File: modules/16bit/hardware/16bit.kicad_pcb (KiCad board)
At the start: 4 copper layers, 29 x 110 mm, 99 parts, among them J1 PJ301M-12, J2 PJ301M-12, J3 PJ301M-12, J4 PJ301M-12, J5 PJ301M-12, J6 Eurorack_2x5, J7 USB-C, Q1 MMBT3904, SW1 MODE, SW2 BOOT, SW3 RUN, U1 RP2350A, U2 W25Q128JVS, U3 APS6404L-3SQR-SN, U4 PT8211, U5 TL074, U6 MCP6002, U7 TL072, U8 AMS1117-5.0, U9 AMS1117-3.3, Y1 12MHz

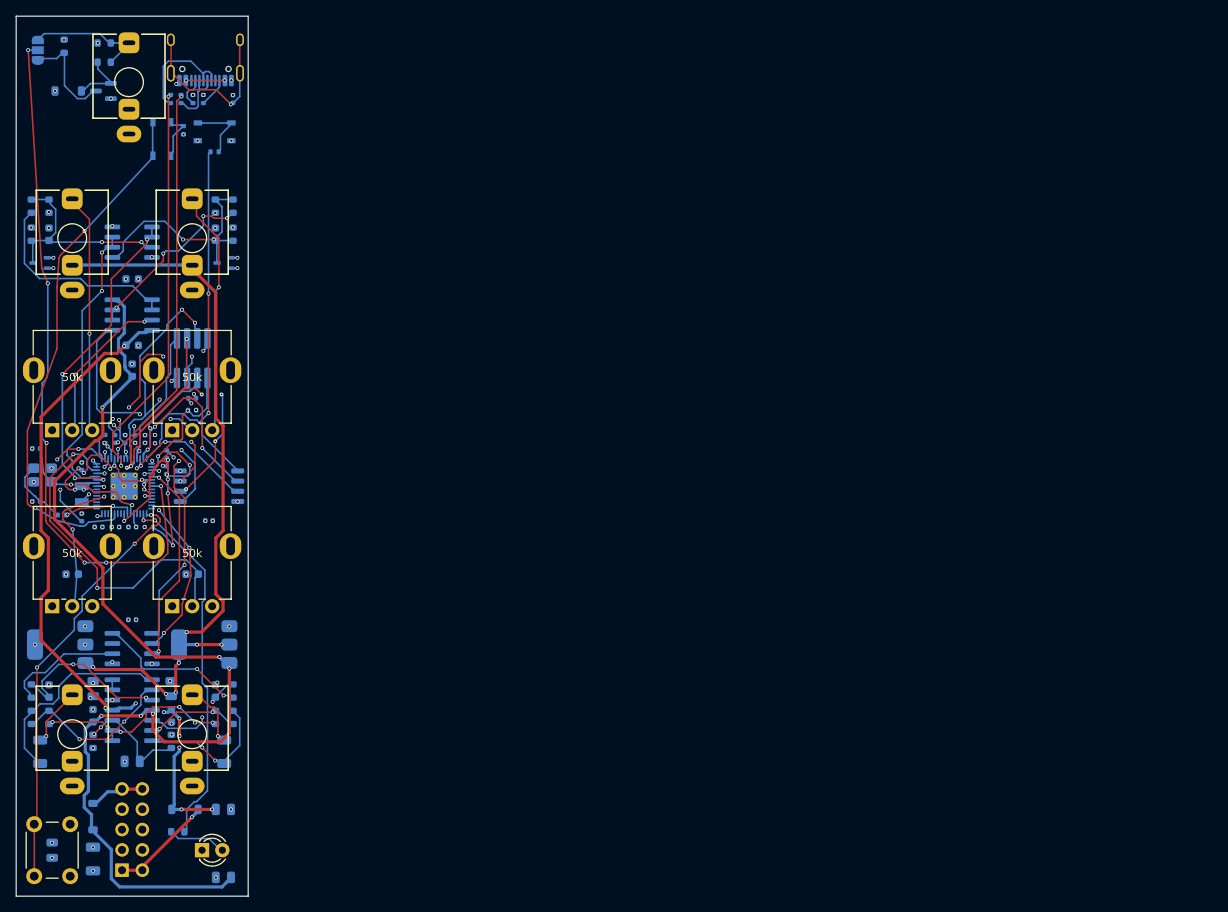
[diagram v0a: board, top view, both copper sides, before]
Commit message: 16bit: start manual re-route; place and route bottom power/output stage
- Strip R1 router copper; move SMD parts off-board for hand placement
- 4-layer stackup (F sig / In1 GND / In2 +3V3 / B sig), Power net class
- Move CV jacks/pots up and to the edge, bottom pots RV3/RV4 to Y128
  (board, panel, geometry.json) to free the middle for the RP2350
- Place and route J6 entry, D2/D3, U8/U9 regulators, U5 output amps,
  VREF divider and outputs to J4/J5 (B.Cu + F.Cu only, no vias in pads)
- Document the no-vias-in-SMD-pads rule for the manual route

Native DRC + schematic parity: 0 violations, 0 parity issues.

Co-Authored-By: Claude Opus 5.5 <noreply@anthropic.com>
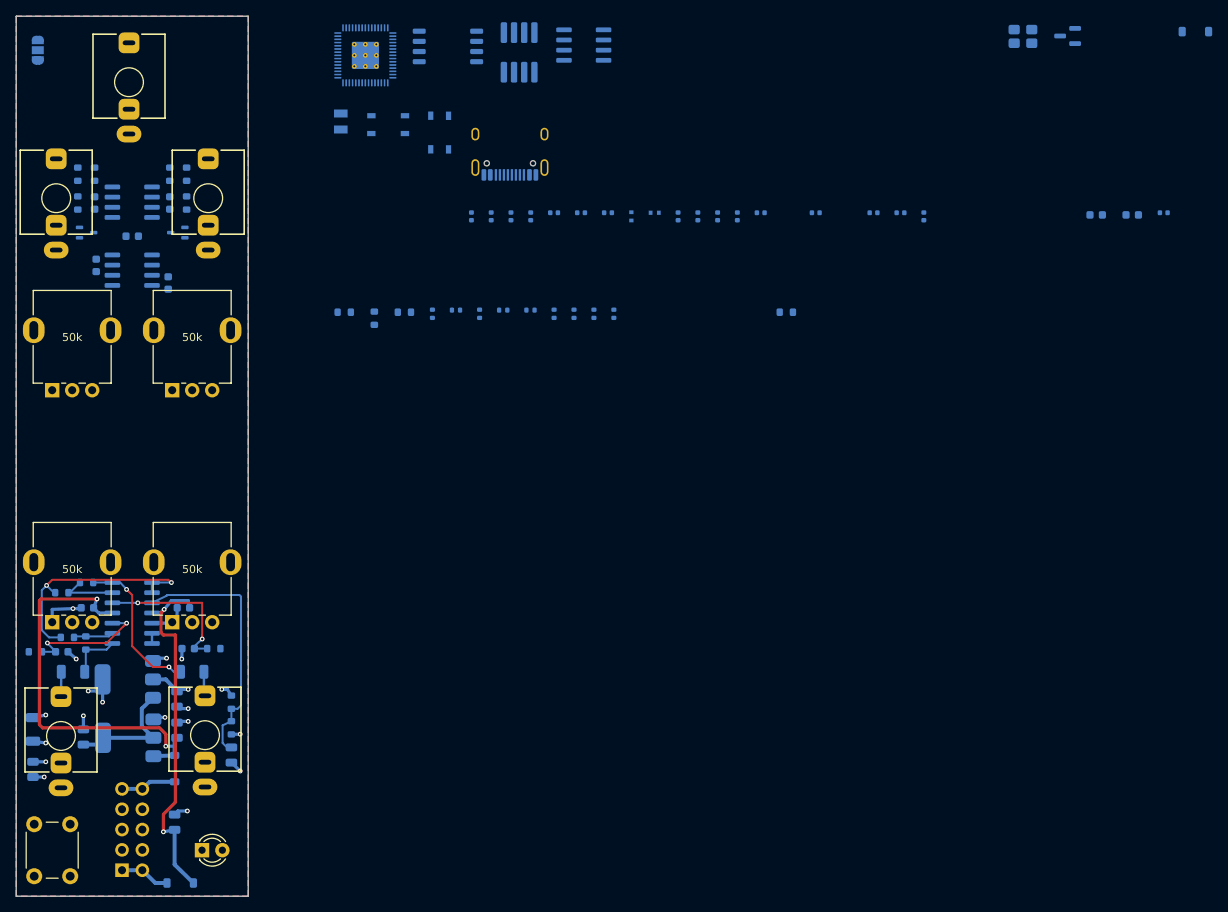
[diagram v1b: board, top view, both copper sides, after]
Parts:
- moved D4 141.1 mm to (247.9, 61.2)
- moved C33 138.6 mm to (243.9, 83.8)
- moved C30 135.6 mm to (235.5, 84.1)
- moved Y1 134.2 mm to (226.3, 61.8)
- moved C31 125.8 mm to (240.0, 84.1)
- moved Q1 120.7 mm to (231.9, 61.7)
- moved C20 103.9 mm to (200.4, 83.8)
- moved R20 100.0 mm to (196.8, 96.2)
- moved C18 95.2 mm to (193.6, 83.8)
- moved U4 94.2 mm to (171.4, 62.9)
- moved C22 91.5 mm to (207.7, 83.8)
- moved C23 91.5 mm to (211.0, 83.8)
- moved C17 90.2 mm to (190.6, 84.3)
- moved C24 87.6 mm to (214.0, 84.3)
- moved C16 85.4 mm to (188.2, 84.3)
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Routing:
- net /MIDI_RX: track 88.3 -> 0.00 mm, vias 6 -> 0
- net +12V_F: track 132.8 -> 50.5 mm, vias 6 -> 2
- net +5V: track 93.4 -> 14.9 mm, vias 7 -> 0
- net +1V1: track 68.7 -> 0.00 mm, vias 16 -> 0
- net /RUN: track 65.4 -> 0.00 mm, vias 2 -> 0
- net /QSPI_SCLK: track 54.2 -> 0.00 mm, vias 7 -> 0
- net /QSPI_SS: track 53.5 -> 0.00 mm, vias 2 -> 0
- net /BUTTON: track 53.4 -> 0.00 mm, vias 3 -> 0
- net /USB_DP: track 50.7 -> 0.00 mm, vias 2 -> 0
- net /USB_DM: track 48.6 -> 0.00 mm, vias 2 -> 0
- net /LED: track 45.5 -> 0.00 mm, vias 2 -> 0
- net /POT4: track 43.8 -> 0.00 mm, vias 2 -> 0
- net /QSPI_SD3: track 42.6 -> 0.00 mm, vias 5 -> 0
- net /QSPI_SD2: track 42.1 -> 0.00 mm, vias 6 -> 0
- net /CV1_ADC: track 41.3 -> 0.00 mm, vias 4 -> 0
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- added copper zone on B.Cu, net GND
- added copper zone on F.Cu, net GND

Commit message: 16bit: add U8 +5V thermal copper (F/B patches, 8 vias)
Co-Authored-By: Claude Opus 5.5 <noreply@anthropic.com>
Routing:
- net +5V: vias 0 -> 8
- added copper zone on B.Cu, net +5V
- added copper zone on F.Cu, net +5V
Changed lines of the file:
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@@
+		)
+	)
+	(via
+		(at 113.5 149.7)
+		(size 0.6)
+		(drill 0.3)
+		(layers "F.Cu" "B.Cu")
+		(net "+5V")
+	)
+	(via
+		(at 115.0 149.7)
+		(size 0.6)
+		(drill 0.3)
+		(layers "F.Cu" "B.Cu")
+		(net "+5V")
+	)
+	(via
+		(at 113.5 151.2)
+		(size 0.6)
+		(drill 0.3)
+		(layers "F.Cu" "B.Cu")
+		(net "+5V")
+	)
+	(via
+		(at 115.0 151.2)
+		(size 0.6)
+		(drill 0.3)
+		(layers "F.Cu" "B.Cu")
+		(net "+5V")
+	)
+	(via
+		(at 113.5 152.7)
+		(size 0.6)
+		(drill 0.3)
+		(layers "F.Cu" "B.Cu")
+		(net "+5V")
+	)
+	(via
+		(at 115.0 152.7)
+		(size 0.6)
+		(drill 0.3)
+		(layers "F.Cu" "B.Cu")
+		(net "+5V")
+	)
+	(via
+		(at 110.5 152.9)
+		(size 0.6)
+		(drill 0.3)
+		(layers "F.Cu" "B.Cu")
+		(net "+5V")
+	)
+	(via
+		(at 112.0 152.9)
+		(size 0.6)
+		(drill 0.3)
+		(layers "F.Cu" "B.Cu")
+		(net "+5V")
+	)
+	(zone
+		(net "+5V")
+		(layer "B.Cu")
+		(name "U8 heat +5V B")
+		(hatch edge 0.5)
+		(priority 1)
+		(connect_pads yes
+			(clearance 0.25)
+		)
+		(min_thickness 0.2)
+		(fill yes
+			(thermal_gap 0.5)
+			(thermal_bridge_width 0.5)
+			(island_removal_mode 0)
+		)
+		(polygon
+			(pts
+				(xy 109.9 145.7) (xy 116.3 145.7) (xy 116.3 154.3) (xy 109.9 154.3)
+			)
+		)
+	)
+	(zone
+		(net "+5V")
+		(layer "F.Cu")
+		(name "U8 heat +5V F")
+		(hatch edge 0.5)
+		(priority 1)
+		(connect_pads yes
+			(clearance 0.25)
+		)
+		(min_thickness 0.2)
+		(fill yes
+			(thermal_gap 0.5)
+			(thermal_bridge_width 0.5)
+			(island_removal_mode 0)
+		)
+		(polygon
+			(pts
+				(xy 108.0 148.75) (xy 118.0 148.75) (xy 118.0 154.3) (xy 108.0 154.3)
+			)
 		)
 	)

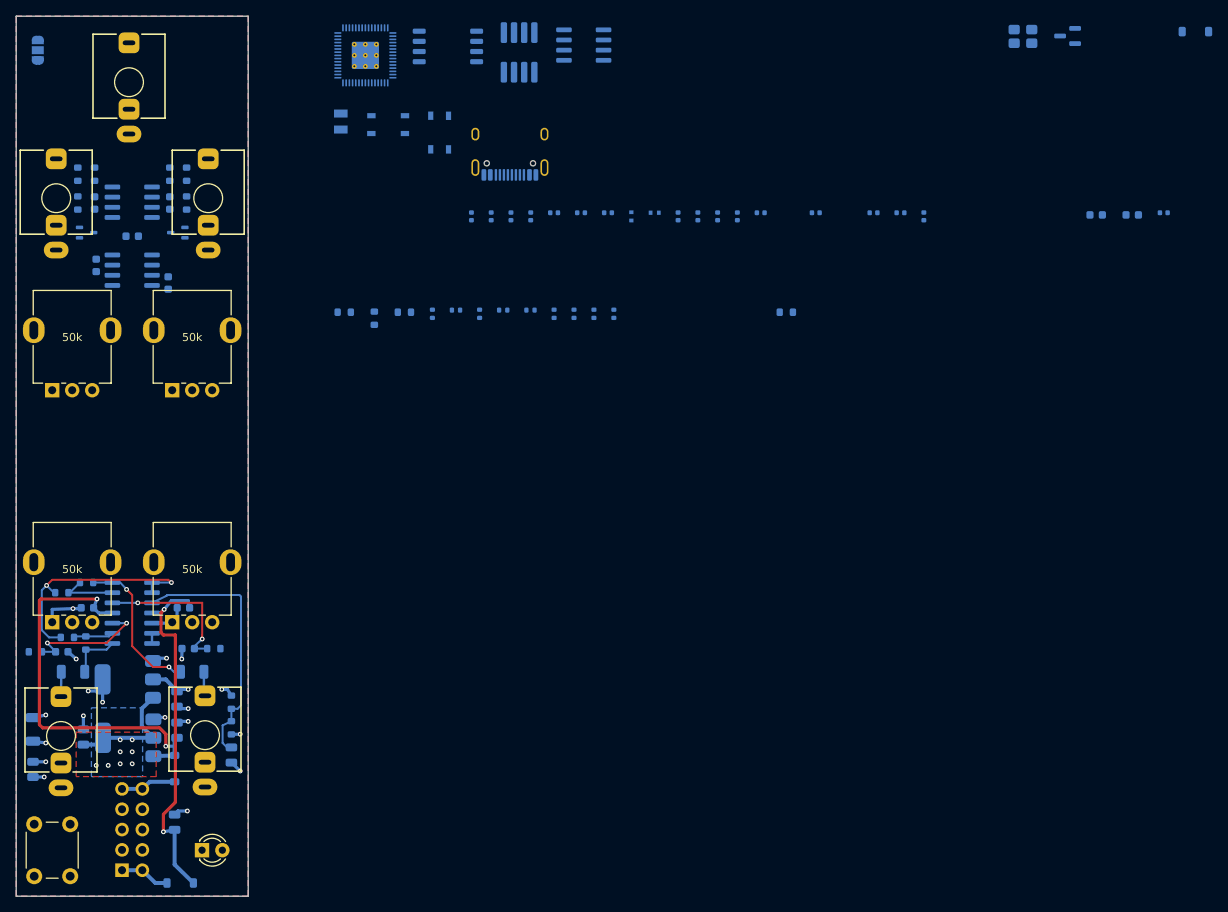
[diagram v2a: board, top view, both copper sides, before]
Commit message: 16bit: place USB-C, MIDI input and CV buffer groups; route their local links
Co-Authored-By: Claude Opus 5.5 <noreply@anthropic.com>
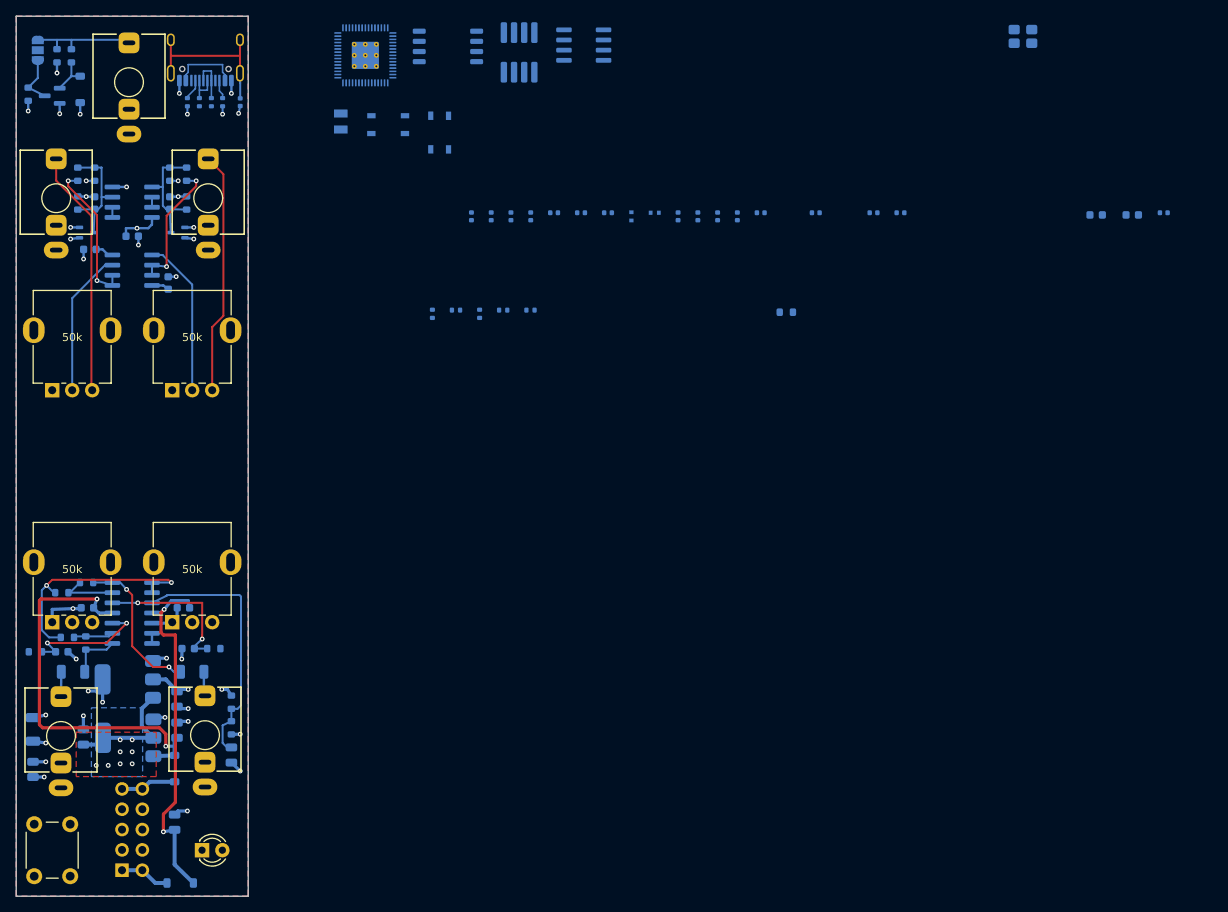
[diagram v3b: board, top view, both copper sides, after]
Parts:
- moved D4 139.6 mm to (108.5, 68.4), turned to -90 degrees
- moved Q1 127.1 mm to (105.0, 69.2)
- moved C24 86.6 mm to (128.5, 70.0), turned to -90 degrees
- moved R11 57.3 mm to (121.9, 70.0), turned to -90 degrees
- moved R12 55.6 mm to (126.3, 70.0), turned to -90 degrees
- moved R3 54.0 mm to (105.6, 64.2), turned to -90 degrees
- moved R10 53.8 mm to (123.4, 70.0), turned to -90 degrees
- moved R2 51.5 mm to (102.0, 69.0), turned to -90 degrees
- moved R9 50.3 mm to (124.9, 70.0), turned to -90 degrees
- moved R1 46.8 mm to (107.4, 64.2), turned to -90 degrees
- moved J7 39.8 mm to (124.2, 63.2)
- moved C29 2.15 mm to (109.7, 88.4), turned to 0 degrees
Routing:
- net /CV1_IN: track 0.00 -> 30.7 mm
- net /CV2_IN: track 0.00 -> 30.3 mm
- net GND: track 26.5 -> 46.9 mm, vias 13 -> 28
- net Net-(J7-SHIELD): track 0.00 -> 20.1 mm
- net Net-(U7B-+): track 0.00 -> 19.8 mm
- net /CV1_AMP: track 0.00 -> 18.4 mm, vias 0 -> 2
- net Net-(U7A-+): track 0.00 -> 18.2 mm
- net /CV2_AMP: track 0.00 -> 16.6 mm, vias 0 -> 2
- net /CV2_BUF: track 0.00 -> 15.2 mm
- net /CV1_BUF: track 0.00 -> 15.2 mm
- net /MIDI_IN: track 0.00 -> 13.9 mm
- net +3V3: track 12.3 -> 24.6 mm, vias 6 -> 13
- net /VBUS: track 0.00 -> 8.54 mm
- net /RX_Q: track 0.00 -> 6.18 mm
- net Net-(J7-D+-PadA6): track 0.00 -> 5.59 mm
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
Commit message: 16bit: place memories, DAC, MCU support, BOOT/RESET; route QSPI, I2S, USB pair, BOOT
- U2 flash / U3 PSRAM beside RP2350, QSPI + PSRAM_CS + I2S on B.Cu with 0 vias
- SW2 BOOT / SW3 RESET at top-left on B.Cu; JP1 MIDI cluster moved 2.6 mm down
- USB D+/D- coupled on F.Cu, 4 vias (2 at port, 2 at MCU)
- U1 regulator corner (L1, C12, C13, C17, R4) and inner power vias
- Native DRC + parity: 0 errors, 2 warnings (unrouted RUN/MIDI_RX escape vias), 40 unconnected

Co-Authored-By: Claude Opus 5.5 <noreply@anthropic.com>
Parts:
- moved Y1 133.2 mm to (108.2, 123.3), turned to -90 degrees
- moved C33 127.9 mm to (124.4, 129.3)
- moved C20 104.6 mm to (104.0, 124.3), turned to -90 degrees
- moved C23 92.3 mm to (126.8, 121.5)
- moved C18 91.4 mm to (110.8, 122.6), turned to -90 degrees
- moved C17 90.7 mm to (104.0, 111.0), turned to 180 degrees
- moved C22 85.9 mm to (127.2, 114.2)
- moved C13 79.5 mm to (104.5, 107.9)
- moved U4 79.1 mm to (122.5, 125.0), turned to -90 degrees
- moved C12 78.9 mm to (102.1, 108.0), turned to 0 degrees
- moved U3 67.2 mm to (123.4, 118.0), turned to 0 degrees
- moved R6 64.8 mm to (102.2, 64.2), turned to 180 degrees
- moved U1 62.5 mm to (108.6, 115.6)
- moved R5 57.1 mm to (105.2, 123.0), turned to -90 degrees
- moved U2 56.9 mm to (123.2, 110.6), turned to 0 degrees
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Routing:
- net Net-(R7-Pad1): track 0.00 -> 67.1 mm, vias 0 -> 2
- net /USB_DP: track 0.00 -> 55.7 mm, vias 0 -> 2
- net /USB_DM: track 0.00 -> 55.4 mm, vias 0 -> 2
- net /QSPI_SD3: track 0.00 -> 42.7 mm
- net /QSPI_SCLK: track 0.00 -> 39.4 mm
- net /QSPI_SD0: track 0.00 -> 31.3 mm
- net GND: track 46.9 -> 72.4 mm, vias 28 -> 41
- net /QSPI_SD2: track 0.00 -> 23.1 mm
- net +3V3: track 24.6 -> 47.6 mm, vias 13 -> 26
- net /I2S_DIN: track 0.00 -> 22.8 mm
- net /QSPI_SD1: track 0.00 -> 21.7 mm
- net /I2S_WS: track 0.00 -> 21.0 mm
- net /I2S_BCK: track 0.00 -> 17.0 mm
- net /PSRAM_CS: track 0.00 -> 16.2 mm
- net +1V1: track 0.00 -> 10.8 mm, vias 0 -> 5
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- added copper zone on F.Cu, net +1V1
